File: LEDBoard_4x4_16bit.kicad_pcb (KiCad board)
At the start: 2 copper layers, 40 x 40 mm, 35 parts, among them J1 signal_in, J2 power, J6 signal_out, U1 TLC5971RGER, U2 TLC5971RGER, U3 TLC5971RGER, U4 TLC5971RGER

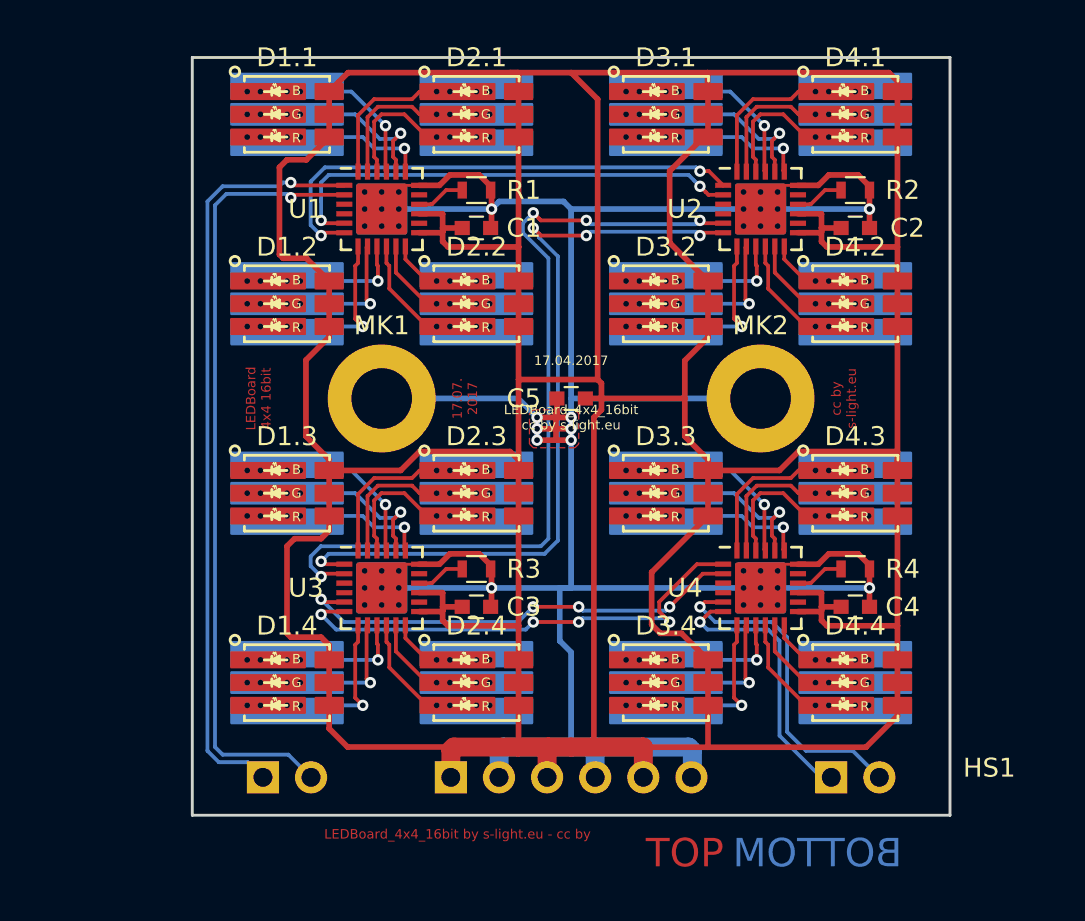
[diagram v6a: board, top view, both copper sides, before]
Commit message: pcb added heatsink 3d model
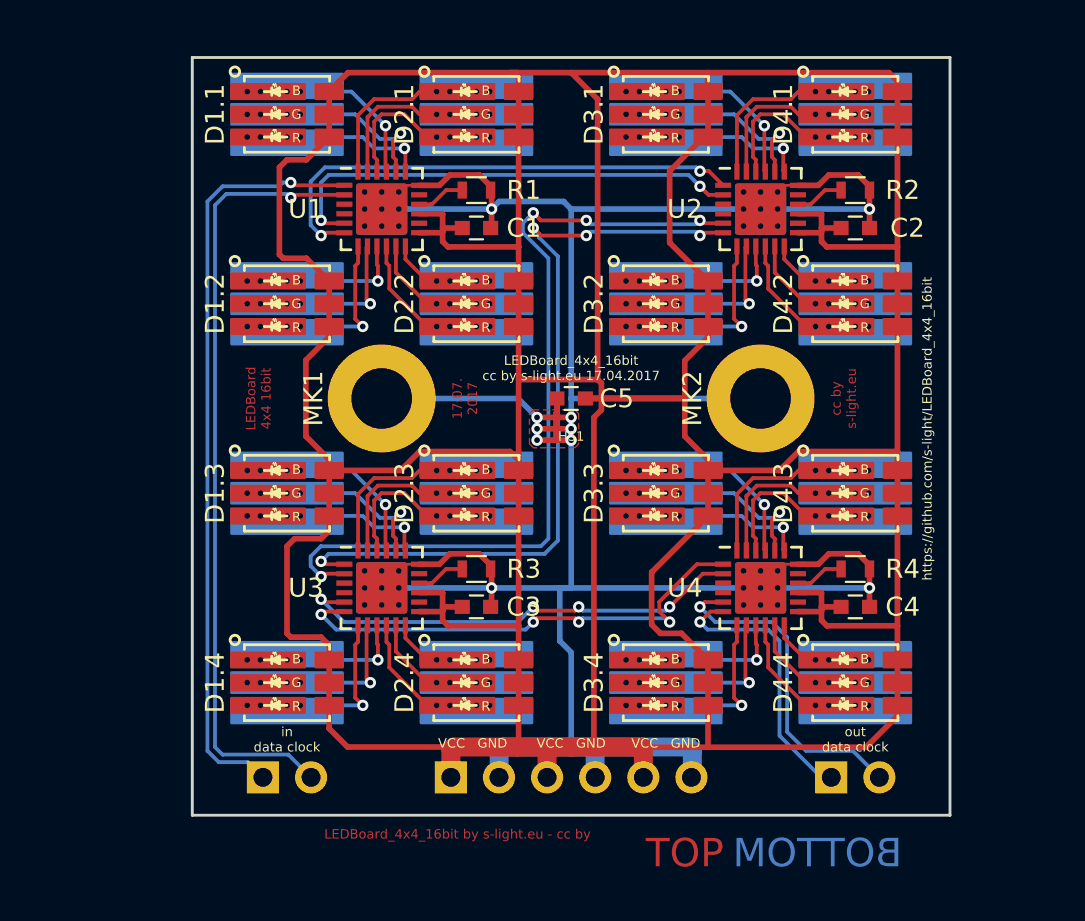
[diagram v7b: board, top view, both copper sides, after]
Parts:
- HS1: moved to B.Cu
- moved HS1 31.1 mm to (70.0, 68.0)
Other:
- board text added: "LEDBoard_4x4_16bit cc by s-light.eu 17.04.2017"
- board text added: "VCC GND"
- board text added: "https://github.com/s-light/LEDBoard_4x4_16bit"
- board text added: "in data clock"
- board text added: "out data clock"
- board text removed: "17.04.2017"
- board text removed: "LEDBoard_4x4_16bit cc by s-light.eu"
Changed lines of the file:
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@@
   (general
     (thickness 1.6)
-    (drawings 29)
-    (tracks 735)
+    (drawings 34)
+    (tracks 739)
     (zones 0)
     (modules 35)
@@
   (page A4)
   (layers
-    (0 F.Cu signal)
-    (31 B.Cu signal)
+    (0 F.Cu signal hide)
+    (31 B.Cu signal hide)
     (32 B.Adhes user)
     (33 F.Adhes user)
@@
     (47 F.CrtYd user)
     (48 B.Fab user)
-    (49 F.Fab user hide)
+    (49 F.Fab user)
   )
   (setup
@@
     (tags "NICHIA, SMD, LED, RGB, Display, White-Binning,")
     (attr smd)
-    (fp_text reference D1.1 (at 0 -3) (layer F.SilkS)
+    (fp_text reference D1.1 (at -3.8 0 90) (layer F.SilkS)
       (effects (font (size 1 1) (thickness 0.15)))
     )
@@
     (tags "NICHIA, SMD, LED, RGB, Display, White-Binning,")
     (attr smd)
-    (fp_text reference D1.2 (at 0 -3) (layer F.SilkS)
+    (fp_text reference D1.2 (at -3.8 0 90) (layer F.SilkS)
       (effects (font (size 1 1) (thickness 0.15)))
     )
@@
     (tags "NICHIA, SMD, LED, RGB, Display, White-Binning,")
     (attr smd)
-    (fp_text reference D1.3 (at 0 -3) (layer F.SilkS)
+    (fp_text reference D1.3 (at -3.8 0 90) (layer F.SilkS)
       (effects (font (size 1 1) (thickness 0.15)))
     )
@@
     (tags "NICHIA, SMD, LED, RGB, Display, White-Binning,")
     (attr smd)
-    (fp_text reference D1.4 (at 0 -3) (layer F.SilkS)
+    (fp_text reference D1.4 (at -3.8 0 90) (layer F.SilkS)
       (effects (font (size 1 1) (thickness 0.15)))
     )
@@
     (tags "NICHIA, SMD, LED, RGB, Display, White-Binning,")
     (attr smd)
-    (fp_text reference D2.1 (at 0 -3) (layer F.SilkS)
+    (fp_text reference D2.1 (at -3.8 0 90) (layer F.SilkS)
       (effects (font (size 1 1) (thickness 0.15)))
     )
@@
     (tags "NICHIA, SMD, LED, RGB, Display, White-Binning,")
     (attr smd)
-    (fp_text reference D2.2 (at 0 -3) (layer F.SilkS)
+    (fp_text reference D2.2 (at -3.8 0 90) (layer F.SilkS)
       (effects (font (size 1 1) (thickness 0.15)))
     )
@@
     (tags "NICHIA, SMD, LED, RGB, Display, White-Binning,")
     (attr smd)
-    (fp_text reference D2.3 (at 0 -3) (layer F.SilkS)
+    (fp_text reference D2.3 (at -3.8 0 90) (layer F.SilkS)
       (effects (font (size 1 1) (thickness 0.15)))
     )
@@
     (tags "NICHIA, SMD, LED, RGB, Display, White-Binning,")
     (attr smd)
-    (fp_text reference D2.4 (at 0 -3) (layer F.SilkS)
+    (fp_text reference D2.4 (at -3.8 0 90) (layer F.SilkS)
       (effects (font (size 1 1) (thickness 0.15)))
     )
@@
     (tags "NICHIA, SMD, LED, RGB, Display, White-Binning,")
     (attr smd)
-    (fp_text reference D3.1 (at 0 -3) (layer F.SilkS)
+    (fp_text reference D3.1 (at -3.8 0 90) (layer F.SilkS)
       (effects (font (size 1 1) (thickness 0.15)))
     )
@@
     (tags "NICHIA, SMD, LED, RGB, Display, White-Binning,")
     (attr smd)
-    (fp_text reference D3.2 (at 0 -3) (layer F.SilkS)
+    (fp_text reference D3.2 (at -3.8 0 90) (layer F.SilkS)
       (effects (font (size 1 1) (thickness 0.15)))
     )
@@
     (tags "NICHIA, SMD, LED, RGB, Display, White-Binning,")
     (attr smd)
-    (fp_text reference D3.3 (at 0 -3) (layer F.SilkS)
+    (fp_text reference D3.3 (at -3.8 0 90) (layer F.SilkS)
       (effects (font (size 1 1) (thickness 0.15)))
     )
@@
     (tags "NICHIA, SMD, LED, RGB, Display, White-Binning,")
     (attr smd)
-    (fp_text reference D3.4 (at 0 -3) (layer F.SilkS)
+    (fp_text reference D3.4 (at -3.8 0 90) (layer F.SilkS)
       (effects (font (size 1 1) (thickness 0.15)))
     )
@@
     (tags "NICHIA, SMD, LED, RGB, Display, White-Binning,")
     (attr smd)
-    (fp_text reference D4.1 (at 0 -3) (layer F.SilkS)
+    (fp_text reference D4.1 (at -3.8 0 90) (layer F.SilkS)
       (effects (font (size 1 1) (thickness 0.15)))
     )
@@
     (tags "NICHIA, SMD, LED, RGB, Display, White-Binning,")
     (attr smd)
-    (fp_text reference D4.2 (at 0 -3) (layer F.SilkS)
+    (fp_text reference D4.2 (at -3.8 0 90) (layer F.SilkS)
       (effects (font (size 1 1) (thickness 0.15)))
     )
@@
     (tags "NICHIA, SMD, LED, RGB, Display, White-Binning,")
     (attr smd)
-    (fp_text reference D4.3 (at 0 -3) (layer F.SilkS)
+    (fp_text reference D4.3 (at -3.8 0 90) (layer F.SilkS)
       (effects (font (size 1 1) (thickness 0.15)))
     )
@@
     (tags "NICHIA, SMD, LED, RGB, Display, White-Binning,")
     (attr smd)
-    (fp_text reference D4.4 (at 0 -3) (layer F.SilkS)
+    (fp_text reference D4.4 (at -3.8 0 90) (layer F.SilkS)
       (effects (font (size 1 1) (thickness 0.15)))
     )
@@
     (descr "Mounting Hole 3.2mm, M3, ISO7380")
     (tags "mounting hole 3.2mm m3 iso7380")
-    (fp_text reference MK1 (at 0 -3.85) (layer F.SilkS)
+    (fp_text reference MK1 (at -3.6 0 90) (layer F.SilkS)
       (effects (font (size 1 1) (thickness 0.15)))
     )
@@
     (pad 1 thru_hole circle (at 0 0) (size 5.7 5.7) (drill 3.2) (layers *.Cu *.Mask)
       (net 2 GND))
-    (model ${KIPRJMOD}/parts/mechanical/screw_M3.step
+    (model ${KIPRJMOD}/parts/mechanical/screw_M3_thinhead.step
       (at (xyz 0 0 0))
       (scale (xyz 1 1 1))
@@
     (tags "capacitor 0603")
     (attr smd)
-    (fp_text reference C5 (at 2.5 0 180) (layer F.SilkS)
+    (fp_text reference C5 (at -2.4 0 180) (layer F.SilkS)
       (effects (font (size 1 1) (thickness 0.15)))
     )
@@
     )
   )
-  (module Oddities:Dummy_Empty (layer F.Cu)
-    (at 92 90)
+  (module Oddities:Dummy_Empty (layer B.Cu)
+    (at 70 68)
     (descr "Only empty Dummy to give satsfaction to DRC")
     (tags "Only empty Dummy to give satsfaction to DRC")
-    (fp_text reference HS1 (at 0.07112 -2.49936) (layer F.SilkS)
-      (effects (font (size 1 1) (thickness 0.15)))
+    (fp_text reference HS1 (at 0 2) (layer F.SilkS)
+      (effects (font (size 0.5 0.5) (thickness 0.1)))
     )
-    (fp_text value Heatsink (at 0 0) (layer F.Fab)
-      (effects (font (size 1 1) (thickness 0.15)))
+    (fp_text value Heatsink (at 0 0) (layer B.Fab)
+      (effects (font (size 1 1) (thickness 0.15)) (justify mirror))
+    )
+    (model ${KIPRJMOD}/parts/mechanical/HeatSink_FischerElektronik__ICK_PGA_14_x_14_x_12.step
+      (at (xyz 0 0 0))
+      (scale (xyz 1 1 1))
+      (rotate (xyz -90 0 0))
     )
   )
@@
     (descr "Mounting Hole 3.2mm, M3, ISO7380")
     (tags "mounting hole 3.2mm m3 iso7380")
-    (fp_text reference MK2 (at 0 -3.85) (layer F.SilkS)
+    (fp_text reference MK2 (at -3.6 0 90) (layer F.SilkS)
       (effects (font (size 1 1) (thickness 0.15)))
     )
@@
     (pad 1 thru_hole circle (at 0 0) (size 5.7 5.7) (drill 3.2) (layers *.Cu *.Mask)
       (net 2 GND))
-    (model ${KIPRJMOD}/parts/mechanical/screw_M3.step
+    (model ${KIPRJMOD}/parts/mechanical/screw_M3_thinhead.step
       (at (xyz 0 0 0))
       (scale (xyz 1 1 1))
@@
     )
   )
+  (gr_text "in\ndata clock" (at 55 86) (layer F.SilkS)
+    (effects (font (size 0.5 0.5) (thickness 0.1)))
+  )
+  (gr_text "out\ndata clock" (at 85 86) (layer F.SilkS)
+    (effects (font (size 0.5 0.5) (thickness 0.1)))
+  )
+  (gr_text "VCC   GND" (at 75 86.2) (layer F.SilkS)
+    (effects (font (size 0.5 0.5) (thickness 0.1)))
+  )
+  (gr_text "VCC   GND" (at 70 86.2) (layer F.SilkS)
+    (effects (font (size 0.5 0.5) (thickness 0.1)))
+  )
+  (gr_text "VCC   GND" (at 64.8 86.2) (layer F.SilkS)
+    (effects (font (size 0.5 0.5) (thickness 0.1)))
+  )
   (gr_text "17.07.\n2017" (at 64.4 68 90) (layer F.Cu)
     (effects (font (size 0.5 0.5) (thickness 0.1)))
@@
     (effects (font (size 0.5 0.5) (thickness 0.1)))
   )
-  (gr_text 17.04.2017 (at 70 66) (layer F.SilkS)
+  (gr_text https://github.com/s-light/LEDBoard_4x4_16bit (at 88.8 69.6 90) (layer F.SilkS)
     (effects (font (size 0.5 0.5) (thickness 0.1)))
   )
-  (gr_text "LEDBoard_4x4_16bit\ncc by s-light.eu" (at 70 69) (layer F.SilkS)
+  (gr_text "LEDBoard_4x4_16bit\ncc by s-light.eu 17.04.2017" (at 70 66.4) (layer F.SilkS)
     (effects (font (size 0.5 0.5) (thickness 0.1)))
   )
@@
   (segment (start 76.6 58.8) (end 71 58.8) (width 0.2) (layer B.Cu) (net 60))
   (segment (start 71 58.8) (end 70.8 58.6) (width 0.2) (layer B.Cu) (net 60))
+  (segment (start 70.4 79) (end 70.2 79.2) (width 0.2) (layer F.Cu) (net 63))
+  (segment (start 70.2 79.2) (end 68.2 79.2) (width 0.2) (layer F.Cu) (net 63))
+  (segment (start 68.2 79.2) (end 68 79) (width 0.2) (layer F.Cu) (net 63))
   (segment (start 75.2 79) (end 75 79.2) (width 0.2) (layer B.Cu) (net 63))
   (segment (start 75 79.2) (end 70.6 79.2) (width 0.2) (layer B.Cu) (net 63))
@@
   (segment (start 77.275 56) (end 77.224284 56) (width 0.2) (layer F.Cu) (net 58))
   (via (at 76.80002 56) (size 0.6) (drill 0.3) (layers F.Cu B.Cu) (net 58))
+  (segment (start 70.4 79.8) (end 70.2 79.6) (width 0.2) (layer F.Cu) (net 75))
+  (segment (start 68.199988 79.6) (end 67.999988 79.8) (width 0.2) (layer F.Cu) (net 75))
+  (segment (start 70.2 79.6) (end 68.199988 79.6) (width 0.2) (layer F.Cu) (net 75))
   (segment (start 75.200012 79.8) (end 75.000012 79.6) (width 0.2) (layer B.Cu) (net 75))
   (segment (start 75.000012 79.6) (end 70.6 79.6) (width 0.2) (layer B.Cu) (net 75))
@@
   (segment (start 67.700001 79.299999) (end 68 79) (width 0.2) (layer B.Cu) (net 63))
   (via (at 68 79) (size 0.6) (drill 0.3) (layers F.Cu B.Cu) (net 63))
-  (segment (start 70.4 79) (end 68 79) (width 0.2) (layer F.Cu) (net 63))
   (via (at 70.4 79) (size 0.6) (drill 0.3) (layers F.Cu B.Cu) (net 63))
   (segment (start 75.2 79) (end 76.95 77.25) (width 0.2) (layer F.Cu) (net 63))
@@
   (via (at 70.4 79.8) (size 0.6) (drill 0.3) (layers F.Cu B.Cu) (net 75))
   (via (at 67.999988 79.8) (size 0.6) (drill 0.3) (layers F.Cu B.Cu) (net 75))
-  (segment (start 70.4 79.8) (end 67.999988 79.8) (width 0.2) (layer F.Cu) (net 75))
   (segment (start 58.025 79.25) (end 56.95 79.25) (width 0.2) (layer F.Cu) (net 75))
   (segment (start 56.95 79.25) (end 56.8 79.4) (width 0.2) (layer F.Cu) (net 75))
